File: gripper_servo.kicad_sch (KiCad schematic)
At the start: 23 parts, among them J20 Conn_01x04_Pin, J21 Conn_01x04_Pin, J22 Conn_01x07, U3 LM2902

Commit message: cleaning up
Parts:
- R11, R5: value R -> 10k
- R13, R19: value R -> 47k
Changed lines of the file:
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@@
       (effects (font (size 1.27 1.27)))
     )
-    (property "Value" "R" (at 182.88 36.83 90)
+    (property "Value" "47k" (at 182.88 36.83 90)
       (effects (font (size 1.27 1.27)))
     )
@@
       (effects (font (size 1.27 1.27)))
     )
-    (property "Value" "R" (at 189.23 114.3 90)
+    (property "Value" "47k" (at 189.23 114.3 90)
       (effects (font (size 1.27 1.27)))
     )
@@
       (effects (font (size 1.27 1.27)))
     )
-    (property "Value" "R" (at 172.72 105.41 90)
+    (property "Value" "10k" (at 172.72 105.41 90)
       (effects (font (size 1.27 1.27)))
     )
@@
       (effects (font (size 1.27 1.27)))
     )
-    (property "Value" "R" (at 172.72 137.16 90)
+    (property "Value" "10k" (at 172.72 137.16 90)
       (effects (font (size 1.27 1.27)))
     )
@@
       (effects (font (size 1.27 1.27)))
     )
-    (property "Value" "R" (at 189.23 146.05 90)
+    (property "Value" "47k" (at 189.23 146.05 90)
       (effects (font (size 1.27 1.27)))
     )
@@
       (effects (font (size 1.27 1.27)))
     )
-    (property "Value" "R" (at 189.23 86.36 90)
+    (property "Value" "47k" (at 189.23 86.36 90)
       (effects (font (size 1.27 1.27)))
     )
@@
       (effects (font (size 1.27 1.27)))
     )
-    (property "Value" "R" (at 172.72 49.53 90)
+    (property "Value" "10k" (at 172.72 49.53 90)
       (effects (font (size 1.27 1.27)))
     )
@@
       (effects (font (size 1.27 1.27)))
     )
-    (property "Value" "R" (at 163.83 36.83 90)
+    (property "Value" "10k" (at 163.83 36.83 90)
       (effects (font (size 1.27 1.27)))
     )
@@
       (effects (font (size 1.27 1.27)))
     )
-    (property "Value" "R" (at 172.72 77.47 90)
+    (property "Value" "10k" (at 172.72 77.47 90)
       (effects (font (size 1.27 1.27)))
     )
@@
       (effects (font (size 1.27 1.27)))
     )
-    (property "Value" "R" (at 189.23 58.42 90)
-      (effects (font (size 1.27 1.27)))
-    )
+    (property "Value" "47k" (at 189.23 58.42 90)
+      (effects (font (size 1.27 1.27)))
+    )

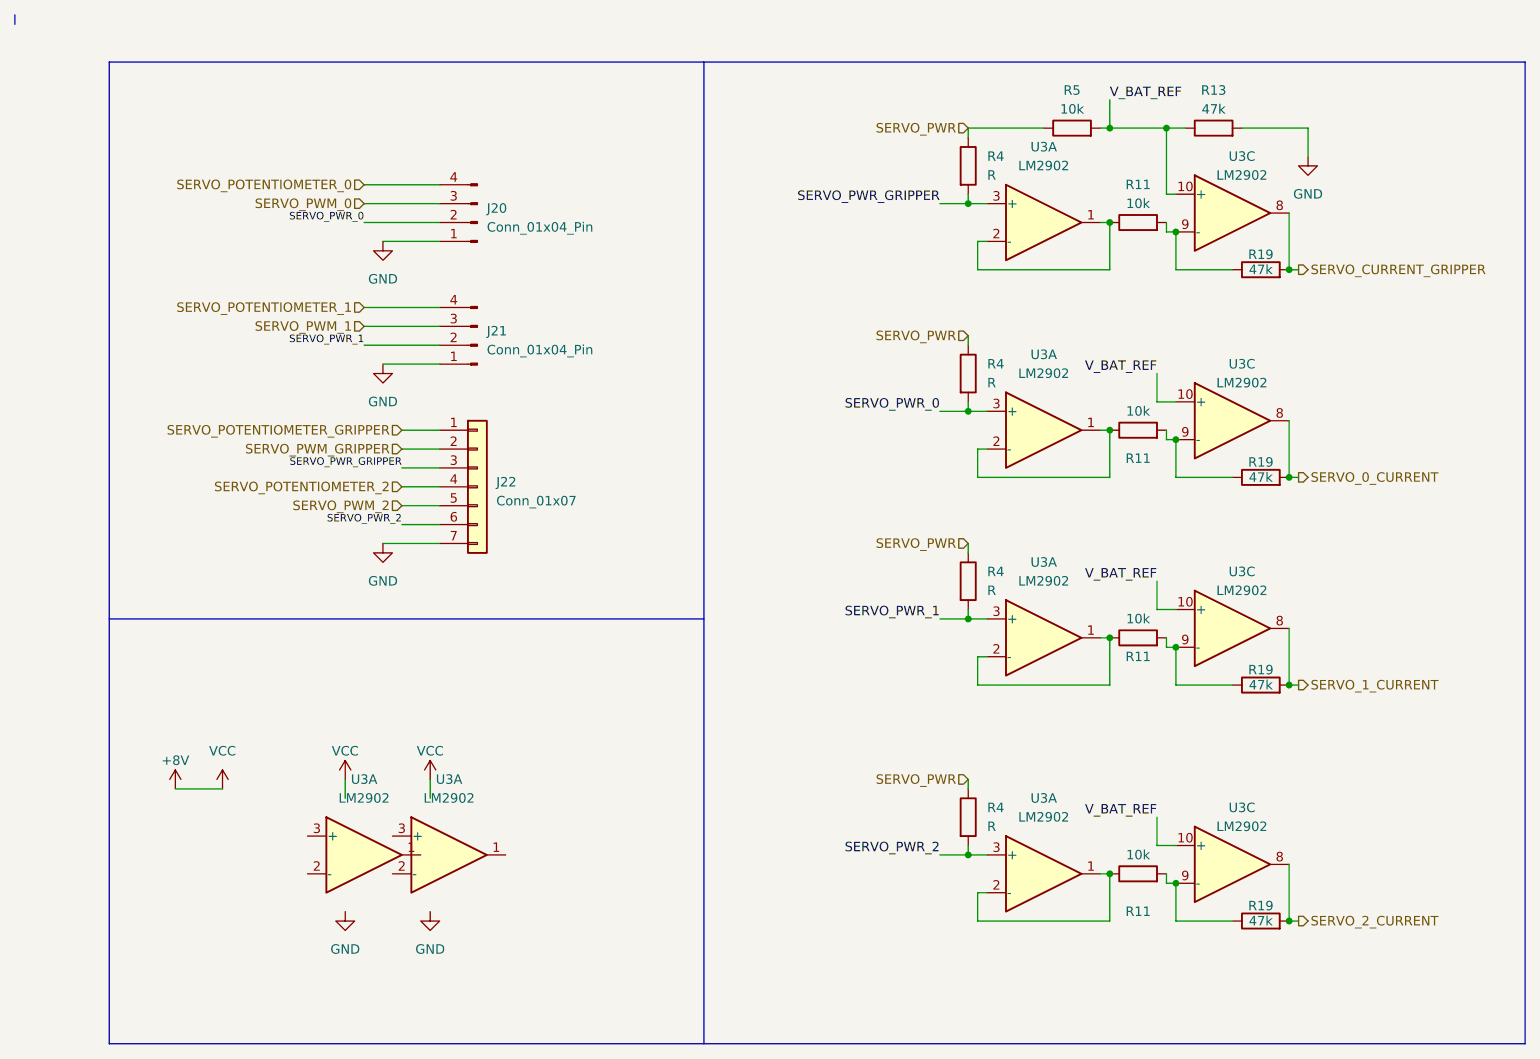
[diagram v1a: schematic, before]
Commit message: Bord v1.2, added flash memory, changed pinout od servomotor connectors and removed potentiometer signal from servomotors plus one ADC
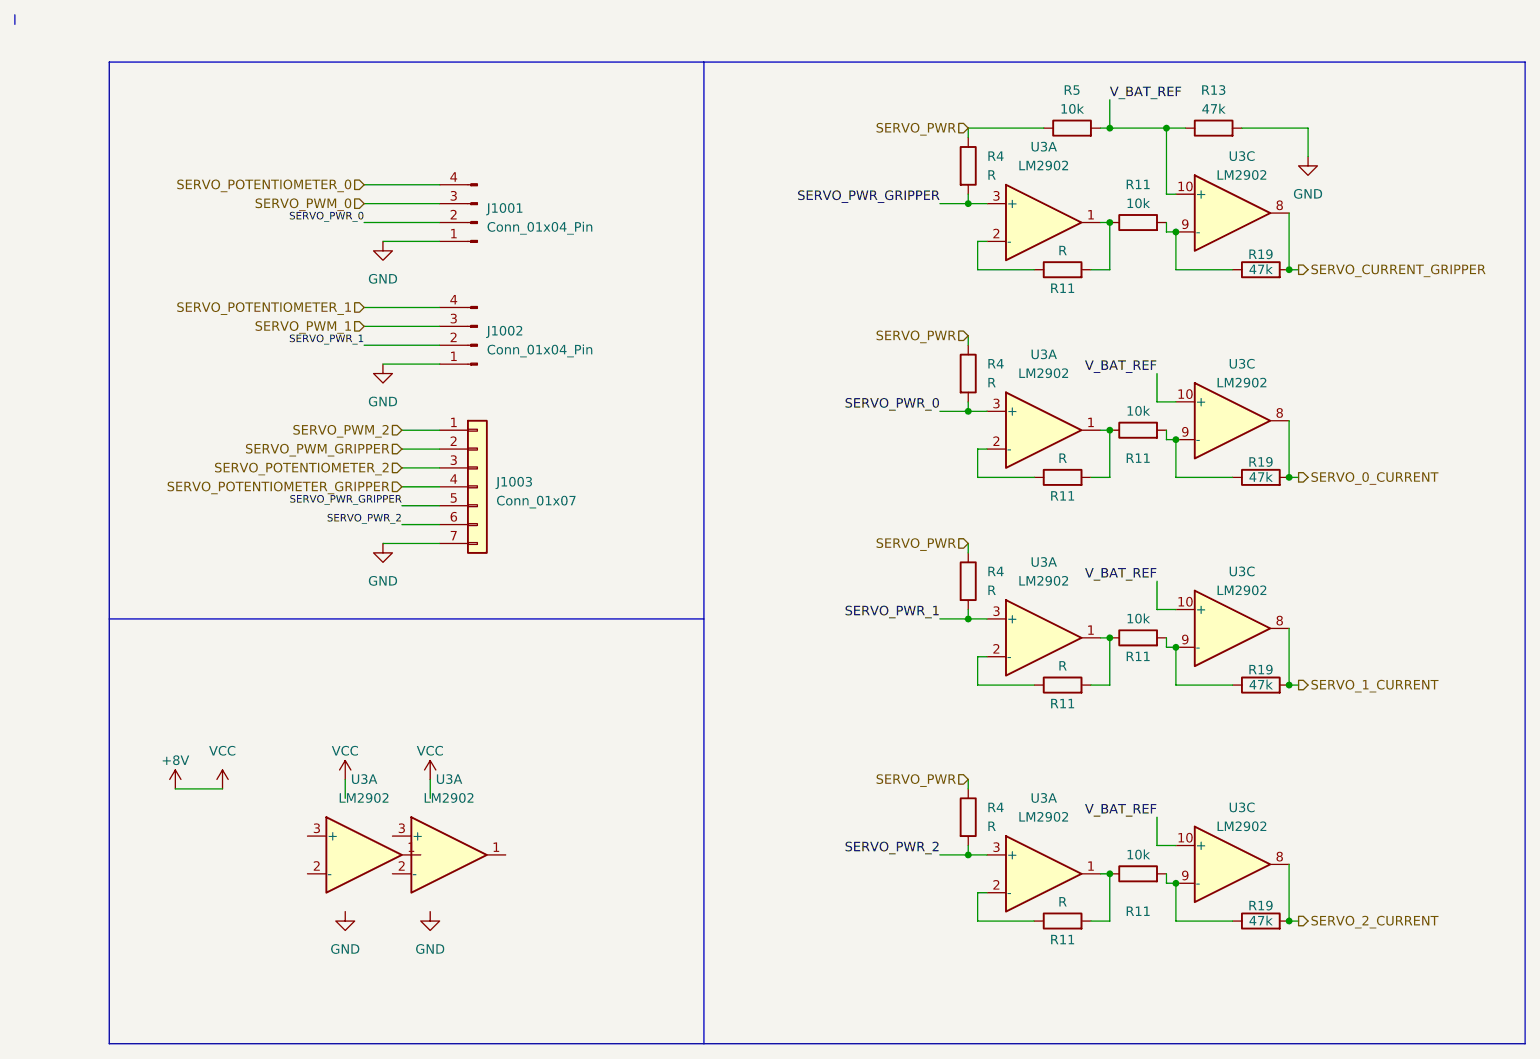
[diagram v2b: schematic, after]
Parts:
- added R11 (x4): R, Resistor_SMD:R_1206_3216Metric_Pad1.30x1.75mm_HandSolder, symbol Device:R
- renumbered J20 to J1001, J21 to J1002, J22 to J1003
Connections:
- net SERVO_POTENTIOMETER_2: now also J1003.3 (Pin_3); no longer J1003.4 (Pin_4)
- net SERVO_POTENTIOMETER_GRIPPER: now also J1003.4 (Pin_4); no longer J1003.1 (Pin_1)
- net SERVO_PWM_2: now also J1003.1 (Pin_1); no longer J1003.5 (Pin_5)
- net SERVO_PWR_GRIPPER: now also J1003.5 (Pin_5); no longer J1003.3 (Pin_3)
- net at R11.1, U3.1: now also R11.2; no longer U3.2 (-) (x4)
- new net: R11.1, U3.2 (-) (x4)
